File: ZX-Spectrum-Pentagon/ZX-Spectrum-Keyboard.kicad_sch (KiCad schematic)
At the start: 130 parts, among them SW1 SW_Push_45deg, SW10 SW_Push_45deg, SW11 SW_Push_45deg, SW12 SW_Push_45deg, SW13 SW_Push_45deg, SW14 SW_Push_45deg, SW15 SW_Push_45deg, SW16 SW_Push_45deg, SW17 SW_Push_45deg, SW18 SW_Push_45deg, SW19 SW_Push_45deg, SW2 SW_Push_45deg, SW20 SW_Push_45deg, SW21 SW_Push_45deg, SW22 SW_Push_45deg, SW23 SW_Push_45deg, SW24 SW_Push_45deg, SW25 SW_Push_45deg, SW26 SW_Push_45deg, SW27 SW_Push_45deg, SW28 SW_Push_45deg, SW29 SW_Push_45deg, SW3 SW_Push_45deg, SW30 SW_Push_45deg, SW31 SW_Push_45deg, SW32 SW_Push_45deg, SW33 SW_Push_45deg, SW34 SW_Push_45deg, SW35 SW_Push_45deg, SW36 SW_Push_45deg, SW37 SW_Push_45deg, SW38 SW_Push_45deg, SW39 SW_Push_45deg, SW4 SW_Push_45deg, SW40 SW_Push_45deg, SW41 SW_Push_45deg, SW42 SW_Push_45deg, SW43 SW_Push_45deg, SW44 SW_Push_45deg, SW45 SW_Push_45deg, SW46 SW_Push_45deg, SW47 SW_Push_45deg, SW48 SW_Push_45deg, SW49 SW_Push_45deg, SW5 SW_Push_45deg, SW50 SW_Push_45deg, SW51 SW_Push_45deg, SW52 SW_Push_45deg, SW53 SW_Push_45deg, SW54 SW_Push_45deg, SW55 SW_Push_45deg, SW56 SW_Push_45deg, SW57 SW_Push_45deg, SW58 SW_Push_45deg, SW6 SW_Push_45deg, SW7 SW_Push_45deg, SW8 SW_Push_45deg, SW9 SW_Push_45deg, U1 74HC32, U2 74HC32, U3 74HC32, U4 74HC32, U5 74HC32, U6 74HC32, U7 74HC32, U8 74HC32

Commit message: improve keyboard
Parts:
- D1, D10, D11, D12, D13, D14, D15, D16, D17, D18, D19, D2, D20, D21, D22, D23, D24, D25, D26, D27, D28, D29, D3, D30, D31, D32, D33, D34, D35, D36, D37, D4, D5, D6, D7, D8, D9: footprint Diode_SMD:D_SOD-323_HandSoldering -> Diode_SMD:D_MiniMELF
- renumbered U6 to U5, U7 to U6, U5 to U6, U6 to U7
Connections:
- net KAR12: now also U5.9 (A), U6.1 (A), U6.9 (A); no longer U5.1 (A), U6.1 (A), U6.9 (A)
- net KAR13: now also U4.9 (A); no longer U4.1 (A)
- net KAR15: now also U4.1 (A), U4.12 (A), U7.1 (A), U7.4 (A); no longer U4.4 (A), U4.9 (A), U7.12 (A), U7.9 (A)
- net KAR8: now also U4.4 (A), U5.12 (A), U6.12 (A), U6.4 (A); no longer U4.12 (A), U5.4 (A), U6.12 (A), U6.4 (A)
- net at D19.2 (K): now also U6.3 (Y); no longer U6.8 (Y)
- net at R11.2, SW51.1: now also U6.2 (B), U6.5 (B); no longer U6.10 (B), U6.13 (B)
- net at R7.2, SW47.1: now also U4.2 (B), U4.5 (B); no longer U4.10 (B), U4.13 (B)
- net at R10.2, SW50.1: now also U5.10 (B), U5.13 (B); no longer U5.2 (B), U5.5 (B)
- net at D22.2 (K): now also U5.11 (Y); no longer U5.6 (Y)
- net at R8.2, SW48.1: now also U4.10 (B), U4.13 (B); no longer U4.2 (B), U4.5 (B)
- net at D16.2 (K): now also U4.11 (Y); no longer U4.6 (Y)
- net at D30.2 (K): now also U7.3 (Y); no longer U7.8 (Y)
- net at D18.2 (K): now also U5.8 (Y); no longer U5.3 (Y)
- net at R12.2, SW52.1: now also U6.10 (B), U6.13 (B); no longer U6.2 (B), U6.5 (B)
- net at D20.2 (K): now also U6.8 (Y); no longer U6.3 (Y)
- net at D12.2 (K): now also U4.8 (Y); no longer U4.3 (Y)
- net at D15.2 (K): now also U4.6 (Y); no longer U4.11 (Y)
- net at D23.2 (K): now also U6.6 (Y); no longer U6.11 (Y)
- net at D34.2 (K): now also U7.6 (Y); no longer U7.11 (Y)
- net at R18.2, SW53.1: now also U7.2 (B), U7.5 (B); no longer U7.10 (B), U7.13 (B)
- net at D24.2 (K): now also U6.11 (Y); no longer U6.6 (Y)
- net at D11.2 (K): now also U4.3 (Y); no longer U4.8 (Y)

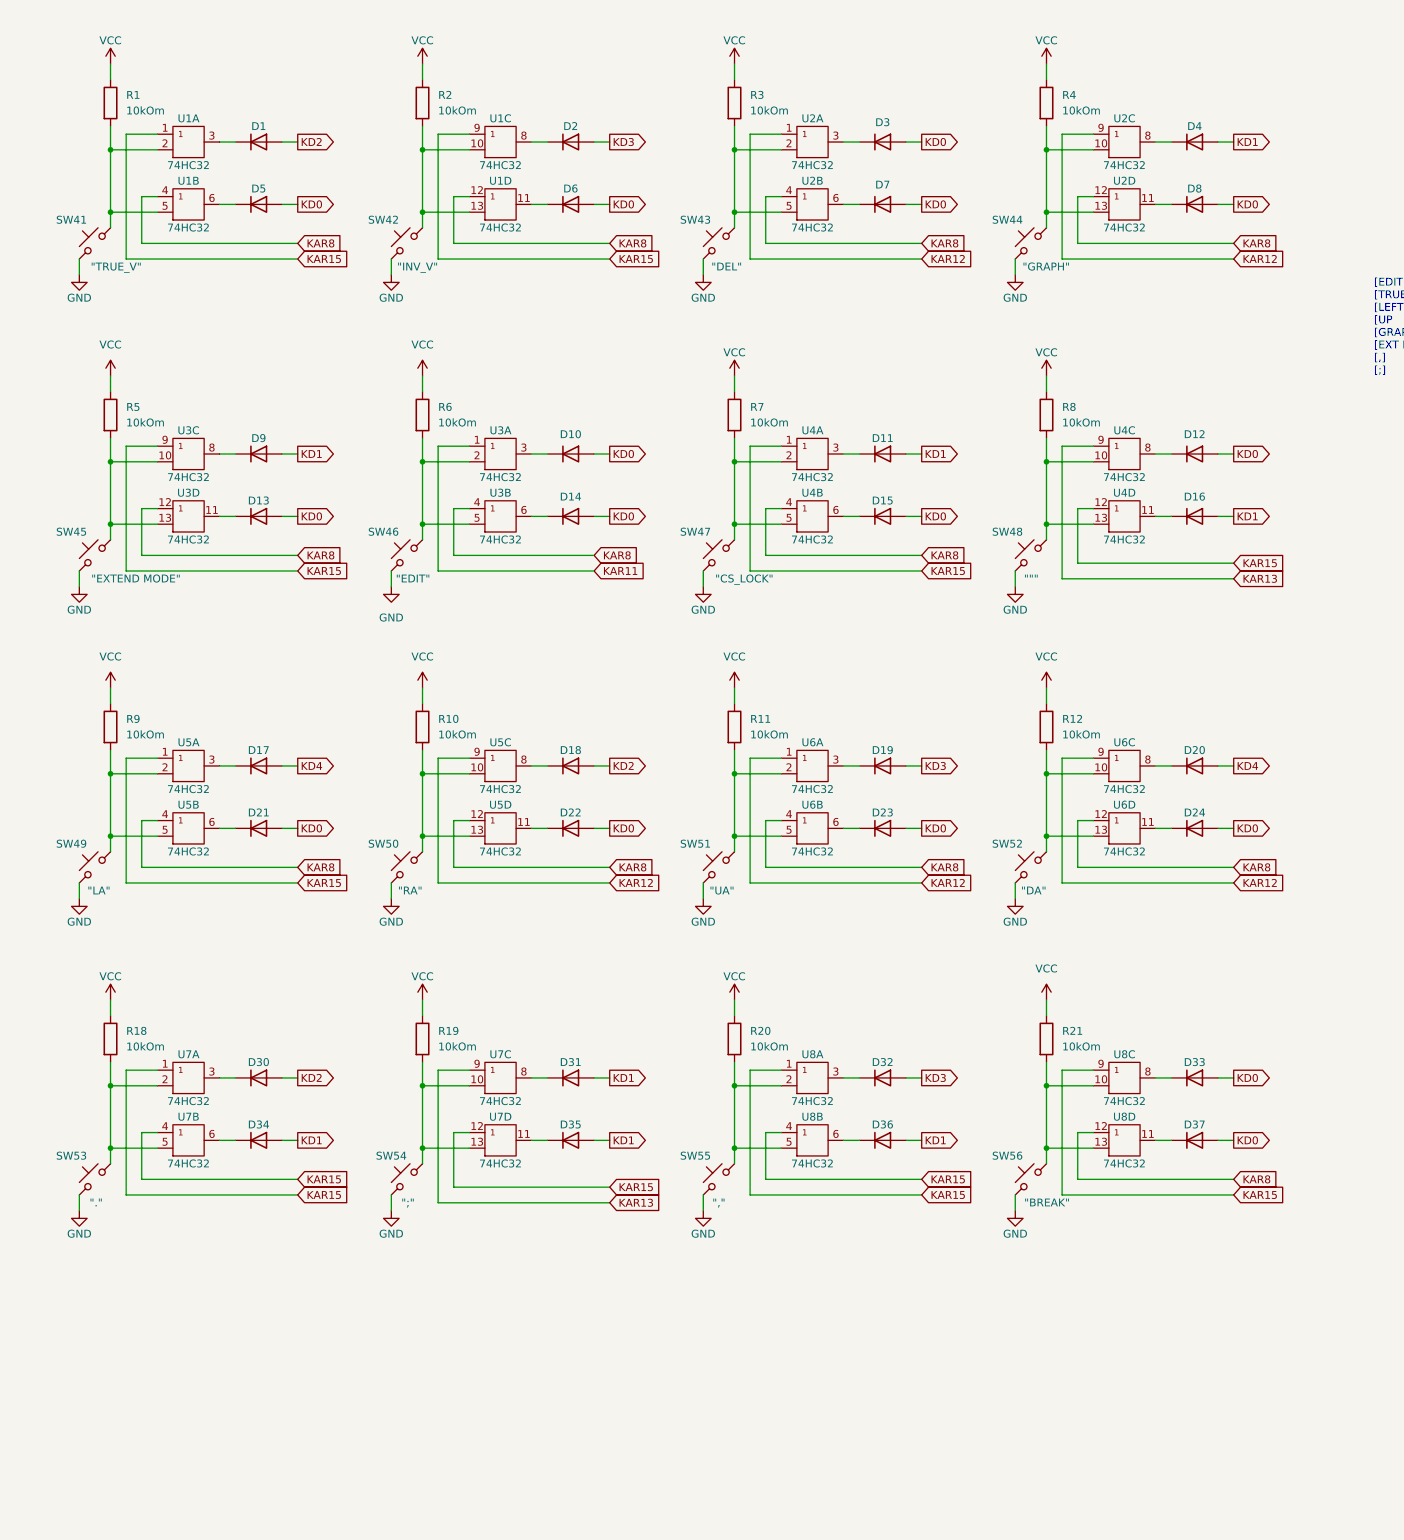
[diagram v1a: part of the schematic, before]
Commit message: update schematic add layout
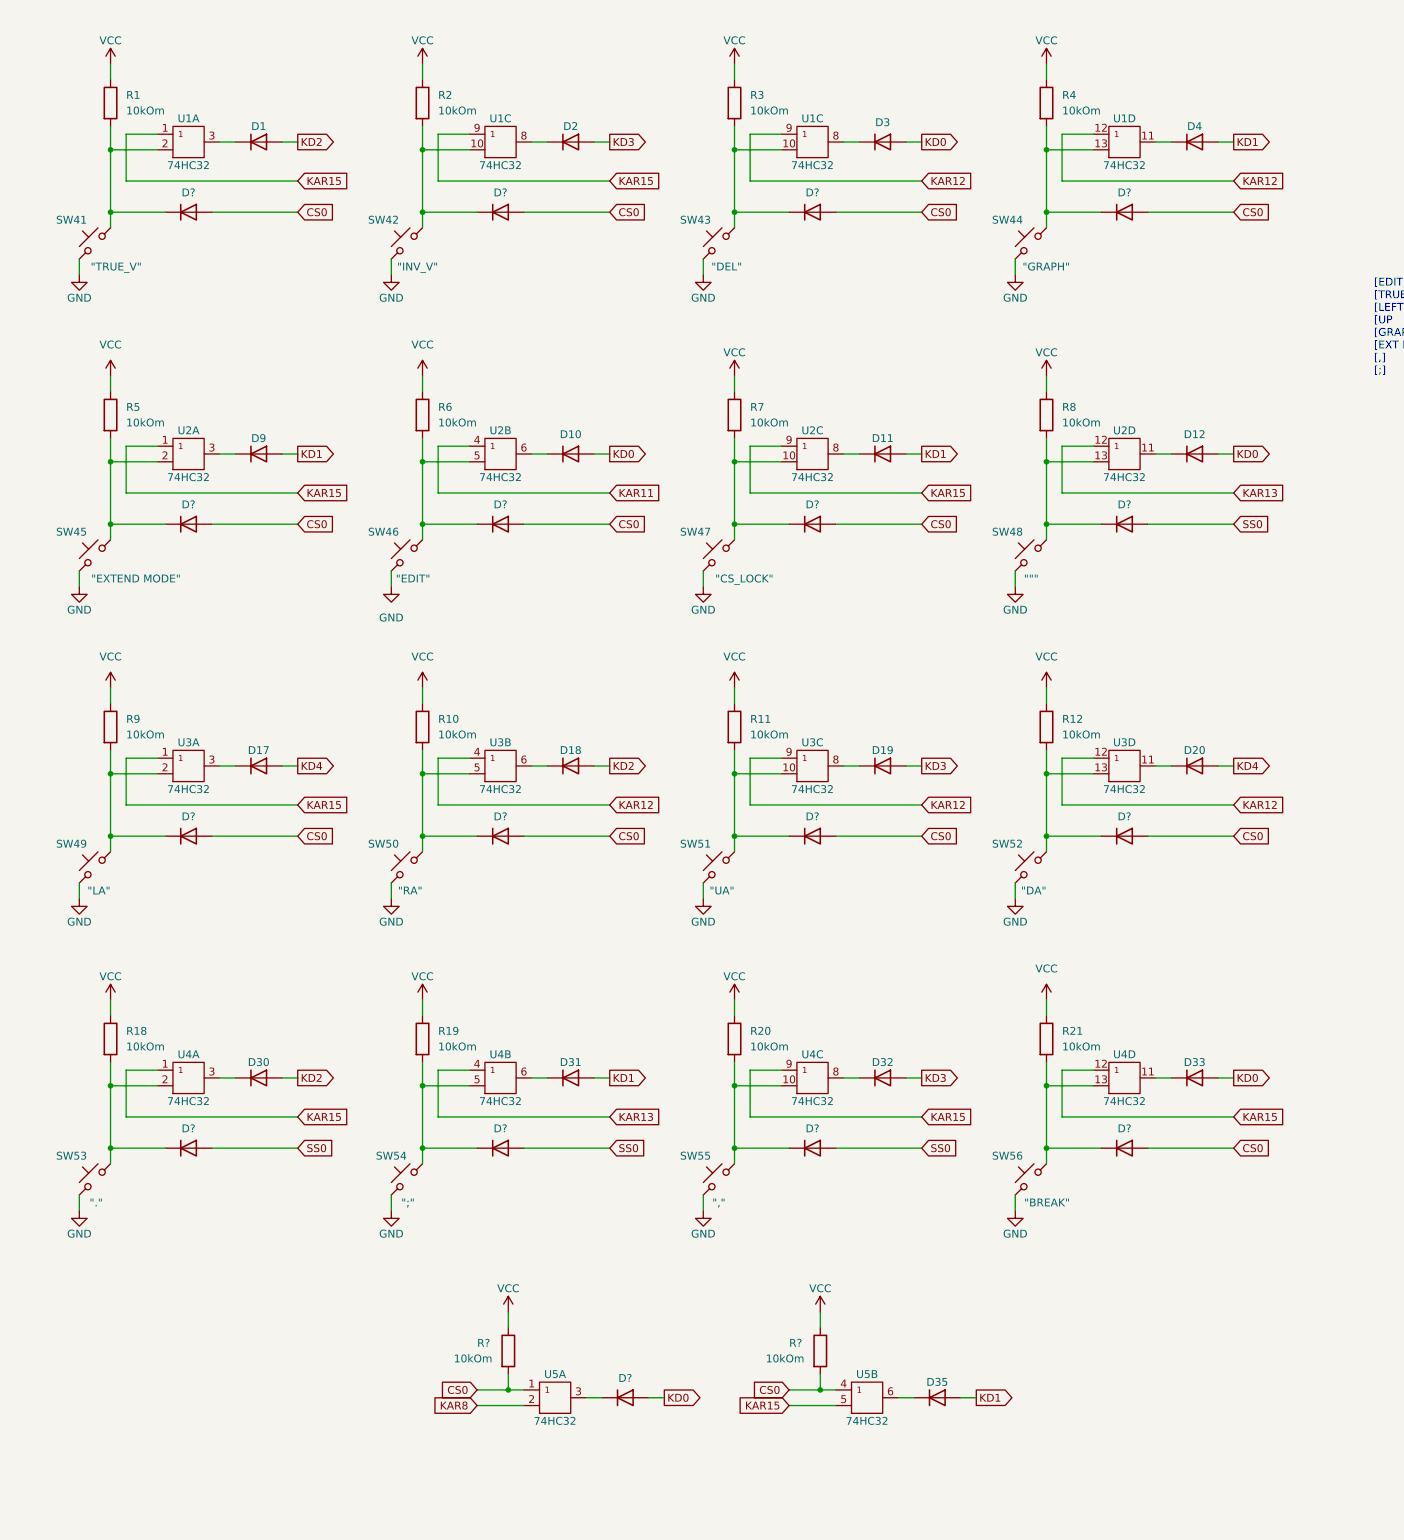
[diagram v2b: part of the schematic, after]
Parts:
- removed D13, D14, D15, D16, D21, D22, D23, D24, D34, D36, D37, D5, D6, D7, D8: 1N4148, Diode_SMD:D_MiniMELF, symbol Simulation_SPICE:DIODE
- removed unit 4 of U1
- removed unit 2 of U1
- removed unit 4 of U2
- removed unit 2 of U2
- removed unit 4 of U3
- removed unit 2 of U3
- removed unit 4 of U4
- removed unit 2 of U4
- removed unit 4 of U5
- removed unit 2 of U5
- removed unit 4 of U6
- removed unit 2 of U6
- removed unit 2 of U7
- removed unit 2 of U8
- removed unit 4 of U8
- added D? (x17): 1N4148, Diode_SMD:D_MiniMELF, symbol Simulation_SPICE:DIODE
- added R? (x2): 10kOm, Resistor_SMD:R_0805_2012Metric_Pad1.20x1.40mm_HandSolder, symbol Device:R
- added unit 1 of U5
- renumbered U2 to U1, U3 to U2, U4 to U2, U5 to U3, U6 to U3, U8 to U4, U7 to U4, U7 to U5
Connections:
- net GND: now also U5.7 (GND)
- net KAR11: now also U2.4 (A); no longer U2.1 (A)
- net KAR12: now also U1.12 (A), U1.9 (A), U3.12 (A), U3.4 (A), U3.9 (A); no longer U1.1 (A), U1.9 (A), U3.1 (A), U3.9 (A), U3.9 (A)
- net KAR13: now also U2.12 (A), U4.4 (A); no longer U2.9 (A), U4.9 (A)
- net KAR15: now also U2.1 (A), U2.9 (A), U4.12 (A), U4.9 (A), U5.5 (B); no longer U2.1 (A), U2.9 (A), U4.1 (A), U4.9 (A), U5.12 (A)
- net KAR8: now also U5.2 (B)
- net KD0: now also D?.1 (A)
- net VCC: now also R?.1, R?.1, U5.14 (VCC)
- net at D19.2 (K): now also U3.8 (Y); no longer U3.3 (Y)
- net at R11.2, SW51.1: now also U3.10 (B), D?.2 (K); no longer U3.2 (B)
- net at R9.2, SW49.1, U3.2 (B): now also D?.2 (K)
- net at R7.2, SW47.1: now also U2.10 (B), D?.2 (K); no longer U2.2 (B)
- net at R4.2, SW44.1: now also U1.13 (B), D?.2 (K); no longer U1.10 (B)
- net at R10.2, SW50.1: now also U3.5 (B), D?.2 (K); no longer U3.10 (B)
- net at R8.2, SW48.1: now also U2.13 (B), D?.2 (K); no longer U2.10 (B)
- net at R1.2, SW41.1, U1.2 (B): now also D?.2 (K)
- net at D4.2 (K): now also U1.11 (Y); no longer U1.8 (Y)
- net at R3.2, SW43.1: now also U1.10 (B), D?.2 (K); no longer U1.2 (B)
- net at D3.2 (K): now also U1.8 (Y); no longer U1.3 (Y)
- net at R5.2, SW45.1: now also U2.2 (B), D?.2 (K); no longer U2.10 (B)
- net at D9.2 (K): now also U2.3 (Y); no longer U2.8 (Y)
- net at D18.2 (K): now also U3.6 (Y); no longer U3.8 (Y)
- net at R19.2, SW54.1: now also U4.5 (B), D?.2 (K); no longer U4.10 (B), U5.13 (B)
- net at R12.2, SW52.1: now also U3.13 (B), D?.2 (K); no longer U3.10 (B)
- net at D20.2 (K): now also U3.11 (Y); no longer U3.8 (Y)
- net at R20.2, SW55.1: now also U4.10 (B), D?.2 (K); no longer U4.2 (B)
- net at R2.2, SW42.1, U1.10 (B): now also D?.2 (K)
- net at D33.2 (K): now also U4.11 (Y); no longer U4.8 (Y)
- net at D10.2 (K): now also U2.6 (Y); no longer U2.3 (Y)
- net at D12.2 (K): now also U2.11 (Y); no longer U2.8 (Y)
- net at D35.2 (K): now also U5.6 (Y); no longer U5.11 (Y)
- net at R21.2, SW56.1: now also U4.13 (B), D?.2 (K); no longer U4.10 (B)
- net at R6.2, SW46.1: now also U2.5 (B), D?.2 (K); no longer U2.2 (B)
- net at R18.2, SW53.1, U4.2 (B): now also D?.2 (K)
- net at D32.2 (K): now also U4.8 (Y); no longer U4.3 (Y)
- net at D31.2 (K): now also U4.6 (Y); no longer U4.8 (Y)
- net at D11.2 (K): now also U2.8 (Y); no longer U2.3 (Y)
- new net: D?.2 (K), U5.3 (Y)
- new net CS0: D?.1 (A), D?.1 (A), D?.1 (A), D?.1 (A), D?.1 (A), D?.1 (A), D?.1 (A), D?.1 (A), D?.1 (A), D?.1 (A), D?.1 (A), D?.1 (A), R?.2, R?.2, U5.1 (A), U5.4 (A)
- new net SS0: D?.1 (A), D?.1 (A), D?.1 (A), D?.1 (A)
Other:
- moved on the sheet: D35, U5B
